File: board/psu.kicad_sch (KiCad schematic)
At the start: 38 parts, among them J1 BARREL_JACK, U1 LTC3374-QFN

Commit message: Continued initial schematic capture
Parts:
- J1: footprint (none) -> azonenberg_pcb:CONN_CUI_PJ-058BH_HIPWR_BARREL_NOSLOT
- R1, R2, R3, R4, R5, R6, R7, R8, R9: footprint (none) -> azonenberg_pcb:EIA_0402_RES_NOSILK
- TP1, TP2: footprint (none) -> azonenberg_pcb:TESTPOINT_SMT_0.5MM
- TP3, TP4, TP5, TP6, TP7: footprint (none) -> azonenberg_pcb:CONN_U.FL_TE_1909763-1
- TP8: footprint (none) -> azonenberg_pcb:TESTPOINT_SMT_KEYSTONE_5016
- U1: footprint (none) -> azonenberg_pcb:QFN_38_0.5MM_5x7MM
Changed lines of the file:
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@@
     (property "Reference" "TP8" (id 0) (at 215.9 123.1605 0))
     (property "Value" "TESTCLIP" (id 1) (at 215.9 125.9356 0))
-    (property "Footprint" "" (id 2) (at 215.9 128.27 0)
+    (property "Footprint" "azonenberg_pcb:TESTPOINT_SMT_KEYSTONE_5016" (id 2) (at 215.9 128.27 0)
       (effects (font (size 1.27 1.27)) hide)
     )
@@
       (effects (font (size 1.524 1.524)))
     )
-    (property "Footprint" "" (id 2) (at 43.18 34.29 0)
+    (property "Footprint" "azonenberg_pcb:QFN_38_0.5MM_5x7MM" (id 2) (at 43.18 34.29 0)
       (effects (font (size 1.524 1.524)) hide)
     )
@@
       (effects (font (size 1.524 1.524)))
     )
-    (property "Footprint" "" (id 2) (at 43.18 176.53 0)
+    (property "Footprint" "azonenberg_pcb:QFN_38_0.5MM_5x7MM" (id 2) (at 43.18 176.53 0)
       (effects (font (size 1.524 1.524)) hide)
     )
@@
       (effects (font (size 1.27 1.27)) (justify left))
     )
-    (property "Footprint" "" (id 2) (at 191.77 158.75 0)
+    (property "Footprint" "azonenberg_pcb:CONN_U.FL_TE_1909763-1" (id 2) (at 191.77 158.75 0)
       (effects (font (size 1.27 1.27)) hide)
     )
@@
     (property "Reference" "R5" (id 0) (at 71.12 114.3 0))
     (property "Value" "806K" (id 1) (at 71.12 116.84 0))
-    (property "Footprint" "" (id 2) (at 77.978 115.57 90)
+    (property "Footprint" "azonenberg_pcb:EIA_0402_RES_NOSILK" (id 2) (at 77.978 115.57 90)
       (effects (font (size 1.27 1.27)) hide)
     )
@@
     (property "Reference" "R1" (id 0) (at 71.12 33.02 0))
     (property "Value" "255K" (id 1) (at 71.12 35.56 0))
-    (property "Footprint" "" (id 2) (at 77.978 34.29 90)
+    (property "Footprint" "azonenberg_pcb:EIA_0402_RES_NOSILK" (id 2) (at 77.978 34.29 90)
       (effects (font (size 1.27 1.27)) hide)
     )
@@
     (property "Reference" "R8" (id 0) (at 71.12 162.56 0))
     (property "Value" "324K" (id 1) (at 71.12 165.1 0))
-    (property "Footprint" "" (id 2) (at 77.978 163.83 90)
+    (property "Footprint" "azonenberg_pcb:EIA_0402_RES_NOSILK" (id 2) (at 77.978 163.83 90)
       (effects (font (size 1.27 1.27)) hide)
     )
@@
     (property "Reference" "J1" (id 0) (at 175.895 17.7505 0))
     (property "Value" "BARREL_JACK" (id 1) (at 175.895 20.5256 0))
-    (property "Footprint" "" (id 2) (at 180.34 29.21 0)
+    (property "Footprint" "azonenberg_pcb:CONN_CUI_PJ-058BH_HIPWR_BARREL_NOSLOT" (id 2) (at 180.34 29.21 0)
       (effects (font (size 1.27 1.27)) hide)
     )
@@
     (property "Reference" "R9" (id 0) (at 201.93 114.3975 90))
     (property "Value" "10K" (id 1) (at 201.93 117.1726 90))
-    (property "Footprint" "" (id 2) (at 201.93 121.158 90)
+    (property "Footprint" "azonenberg_pcb:EIA_0402_RES_NOSILK" (id 2) (at 201.93 121.158 90)
       (effects (font (size 1.27 1.27)) hide)
     )
@@
       (effects (font (size 1.524 1.524)))
     )
-    (property "Footprint" "" (id 2) (at 43.18 156.21 0)
+    (property "Footprint" "azonenberg_pcb:QFN_38_0.5MM_5x7MM" (id 2) (at 43.18 156.21 0)
       (effects (font (size 1.524 1.524)) hide)
     )
@@
       (effects (font (size 1.524 1.524)))
     )
-    (property "Footprint" "" (id 2) (at 43.18 115.57 0)
+    (property "Footprint" "azonenberg_pcb:QFN_38_0.5MM_5x7MM" (id 2) (at 43.18 115.57 0)
       (effects (font (size 1.524 1.524)) hide)
     )
@@
       (effects (font (size 1.524 1.524)))
     )
-    (property "Footprint" "" (id 2) (at 43.18 54.61 0)
+    (property "Footprint" "azonenberg_pcb:QFN_38_0.5MM_5x7MM" (id 2) (at 43.18 54.61 0)
       (effects (font (size 1.524 1.524)) hide)
     )
@@
     (property "Reference" "R7" (id 0) (at 71.12 154.94 0))
     (property "Value" "1.02M" (id 1) (at 71.12 157.48 0))
-    (property "Footprint" "" (id 2) (at 77.978 156.21 90)
+    (property "Footprint" "azonenberg_pcb:EIA_0402_RES_NOSILK" (id 2) (at 77.978 156.21 90)
       (effects (font (size 1.27 1.27)) hide)
     )
@@
     (property "Reference" "TP2" (id 0) (at 184.15 123.1605 0))
     (property "Value" "TESTPOINT" (id 1) (at 184.15 125.9356 0))
-    (property "Footprint" "" (id 2) (at 184.15 128.27 0)
+    (property "Footprint" "azonenberg_pcb:TESTPOINT_SMT_0.5MM" (id 2) (at 184.15 128.27 0)
       (effects (font (size 1.27 1.27)) hide)
     )
@@
       (effects (font (size 1.27 1.27)) (justify left))
     )
-    (property "Footprint" "" (id 2) (at 191.77 168.91 0)
+    (property "Footprint" "azonenberg_pcb:CONN_U.FL_TE_1909763-1" (id 2) (at 191.77 168.91 0)
       (effects (font (size 1.27 1.27)) hide)
     )
@@
       (effects (font (size 1.27 1.27)) (justify left))
     )
-    (property "Footprint" "" (id 2) (at 191.77 179.07 0)
+    (property "Footprint" "azonenberg_pcb:CONN_U.FL_TE_1909763-1" (id 2) (at 191.77 179.07 0)
       (effects (font (size 1.27 1.27)) hide)
     )
@@
     (property "Reference" "TP1" (id 0) (at 184.15 114.2705 0))
     (property "Value" "TESTPOINT" (id 1) (at 184.15 117.0456 0))
-    (property "Footprint" "" (id 2) (at 184.15 119.38 0)
+    (property "Footprint" "azonenberg_pcb:TESTPOINT_SMT_0.5MM" (id 2) (at 184.15 119.38 0)
       (effects (font (size 1.27 1.27)) hide)
     )
@@
     (property "Reference" "R4" (id 0) (at 71.12 81.28 0))
     (property "Value" "464K" (id 1) (at 71.12 83.82 0))
-    (property "Footprint" "" (id 2) (at 77.978 82.55 90)
+    (property "Footprint" "azonenberg_pcb:EIA_0402_RES_NOSILK" (id 2) (at 77.978 82.55 90)
       (effects (font (size 1.27 1.27)) hide)
     )
@@
       (effects (font (size 1.524 1.524)))
     )
-    (property "Footprint" "" (id 2) (at 43.18 135.89 0)
+    (property "Footprint" "azonenberg_pcb:QFN_38_0.5MM_5x7MM" (id 2) (at 43.18 135.89 0)
       (effects (font (size 1.524 1.524)) hide)
     )
@@
       (effects (font (size 1.524 1.524)))
     )
-    (property "Footprint" "" (id 2) (at 43.18 74.93 0)
+    (property "Footprint" "azonenberg_pcb:QFN_38_0.5MM_5x7MM" (id 2) (at 43.18 74.93 0)
       (effects (font (size 1.524 1.524)) hide)
     )
@@
       (effects (font (size 1.27 1.27)) (justify left))
     )
-    (property "Footprint" "" (id 2) (at 191.77 148.59 0)
+    (property "Footprint" "azonenberg_pcb:CONN_U.FL_TE_1909763-1" (id 2) (at 191.77 148.59 0)
       (effects (font (size 1.27 1.27)) hide)
     )
@@
       (effects (font (size 1.524 1.524)))
     )
-    (property "Footprint" "" (id 2) (at 43.18 95.25 0)
+    (property "Footprint" "azonenberg_pcb:QFN_38_0.5MM_5x7MM" (id 2) (at 43.18 95.25 0)
       (effects (font (size 1.524 1.524)) hide)
     )
@@
       (effects (font (size 1.27 1.27)) (justify left))
     )
-    (property "Footprint" "" (id 2) (at 191.77 138.43 0)
+    (property "Footprint" "azonenberg_pcb:CONN_U.FL_TE_1909763-1" (id 2) (at 191.77 138.43 0)
       (effects (font (size 1.27 1.27)) hide)
     )
@@
     (property "Reference" "R3" (id 0) (at 71.12 73.66 0))
     (property "Value" "232K" (id 1) (at 71.12 76.2 0))
-    (property "Footprint" "" (id 2) (at 77.978 74.93 90)
+    (property "Footprint" "azonenberg_pcb:EIA_0402_RES_NOSILK" (id 2) (at 77.978 74.93 90)
       (effects (font (size 1.27 1.27)) hide)
     )
@@
     (property "Reference" "R6" (id 0) (at 71.12 121.92 0))
     (property "Value" "649K" (id 1) (at 71.12 124.46 0))
-    (property "Footprint" "" (id 2) (at 77.978 123.19 90)
+    (property "Footprint" "azonenberg_pcb:EIA_0402_RES_NOSILK" (id 2) (at 77.978 123.19 90)
       (effects (font (size 1.27 1.27)) hide)
     )
@@
       (effects (font (size 1.524 1.524)))
     )
-    (property "Footprint" "" (id 2) (at 138.43 34.29 0)
+    (property "Footprint" "azonenberg_pcb:QFN_38_0.5MM_5x7MM" (id 2) (at 138.43 34.29 0)
       (effects (font (size 1.524 1.524)) hide)
     )
@@
     (property "Reference" "R2" (id 0) (at 71.12 40.64 0))
     (property "Value" "1.02M" (id 1) (at 71.12 43.18 0))
-    (property "Footprint" "" (id 2) (at 77.978 41.91 90)
-      (effects (font (size 1.27 1.27)) hide)
-    )
+    (property "Footprint" "azonenberg_pcb:EIA_0402_RES_NOSILK" (id 2) (at 77.978 41.91 90)
+      (effects (font (size 1.27 1.27)) hide)
+    )

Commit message: Finished initial schematic, ready for signoff review
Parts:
- C1, C10, C11, C12, C13, C14, C2, C4, C6, C7, C8, C9: footprint (none) -> azonenberg_pcb:EIA_1210_CAP_NOSILK
- C3, C5: footprint (none) -> azonenberg_pcb:EIA_1206_CAP_NOSILK
- F1: footprint (none) -> azonenberg_pcb:EIA_0603_CAP_NOSILK
- L1, L2, L3, L4: footprint (none) -> azonenberg_pcb:INDUCTOR_YUDEN_NRS5030
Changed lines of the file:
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@@
       (effects (font (size 1.27 1.27)) (justify left))
     )
-    (property "Footprint" "" (id 2) (at 82.2452 160.02 0)
+    (property "Footprint" "azonenberg_pcb:EIA_1210_CAP_NOSILK" (id 2) (at 82.2452 160.02 0)
       (effects (font (size 1.27 1.27)) hide)
     )
@@
       (effects (font (size 1.016 1.016)))
     )
-    (property "Footprint" "" (id 2) (at 64.77 71.12 0)
+    (property "Footprint" "azonenberg_pcb:INDUCTOR_YUDEN_NRS5030" (id 2) (at 64.77 71.12 0)
       (effects (font (size 1.524 1.524)) hide)
     )
@@
       (effects (font (size 1.27 1.27)) (justify left))
     )
-    (property "Footprint" "" (id 2) (at 89.8652 190.5 0)
+    (property "Footprint" "azonenberg_pcb:EIA_1210_CAP_NOSILK" (id 2) (at 89.8652 190.5 0)
       (effects (font (size 1.27 1.27)) hide)
     )
@@
       (effects (font (size 1.27 1.27)) (justify left))
     )
-    (property "Footprint" "" (id 2) (at 82.2452 78.74 0)
+    (property "Footprint" "azonenberg_pcb:EIA_1210_CAP_NOSILK" (id 2) (at 82.2452 78.74 0)
       (effects (font (size 1.27 1.27)) hide)
     )
@@
       (effects (font (size 1.27 1.27)) (justify left))
     )
-    (property "Footprint" "" (id 2) (at 55.5752 190.5 0)
+    (property "Footprint" "azonenberg_pcb:EIA_1210_CAP_NOSILK" (id 2) (at 55.5752 190.5 0)
       (effects (font (size 1.27 1.27)) hide)
     )
@@
       (effects (font (size 1.27 1.27)) (justify left))
     )
-    (property "Footprint" "" (id 2) (at 207.9752 30.48 0)
+    (property "Footprint" "azonenberg_pcb:EIA_1206_CAP_NOSILK" (id 2) (at 207.9752 30.48 0)
       (effects (font (size 1.27 1.27)) hide)
     )
@@
       (effects (font (size 1.27 1.27)) (justify left))
     )
-    (property "Footprint" "" (id 2) (at 32.7152 190.5 0)
+    (property "Footprint" "azonenberg_pcb:EIA_1210_CAP_NOSILK" (id 2) (at 32.7152 190.5 0)
       (effects (font (size 1.27 1.27)) hide)
     )
@@
       (effects (font (size 1.27 1.27)) (justify left))
     )
-    (property "Footprint" "" (id 2) (at 21.2852 190.5 0)
+    (property "Footprint" "azonenberg_pcb:EIA_1210_CAP_NOSILK" (id 2) (at 21.2852 190.5 0)
       (effects (font (size 1.27 1.27)) hide)
     )
@@
       (effects (font (size 1.27 1.27)) (justify left))
     )
-    (property "Footprint" "" (id 2) (at 112.7252 190.5 0)
+    (property "Footprint" "azonenberg_pcb:EIA_1210_CAP_NOSILK" (id 2) (at 112.7252 190.5 0)
       (effects (font (size 1.27 1.27)) hide)
     )
@@
       (effects (font (size 1.27 1.27)) (justify left))
     )
-    (property "Footprint" "" (id 2) (at 82.2452 38.1 0)
+    (property "Footprint" "azonenberg_pcb:EIA_1210_CAP_NOSILK" (id 2) (at 82.2452 38.1 0)
       (effects (font (size 1.27 1.27)) hide)
     )
@@
       (effects (font (size 1.27 1.27)) (justify left))
     )
-    (property "Footprint" "" (id 2) (at 67.0052 190.5 0)
+    (property "Footprint" "azonenberg_pcb:EIA_1210_CAP_NOSILK" (id 2) (at 67.0052 190.5 0)
       (effects (font (size 1.27 1.27)) hide)
     )
@@
       (effects (font (size 1.27 1.27)) (justify left))
     )
-    (property "Footprint" "" (id 2) (at 82.2452 119.38 0)
+    (property "Footprint" "azonenberg_pcb:EIA_1206_CAP_NOSILK" (id 2) (at 82.2452 119.38 0)
       (effects (font (size 1.27 1.27)) hide)
     )
@@
       (effects (font (size 1.016 1.016)))
     )
-    (property "Footprint" "" (id 2) (at 64.77 152.4 0)
+    (property "Footprint" "azonenberg_pcb:INDUCTOR_YUDEN_NRS5030" (id 2) (at 64.77 152.4 0)
       (effects (font (size 1.524 1.524)) hide)
     )
@@
       (effects (font (size 1.27 1.27)) (justify left))
     )
-    (property "Footprint" "" (id 2) (at 101.2952 190.5 0)
+    (property "Footprint" "azonenberg_pcb:EIA_1210_CAP_NOSILK" (id 2) (at 101.2952 190.5 0)
       (effects (font (size 1.27 1.27)) hide)
     )
@@
       (effects (font (size 1.27 1.27)) (justify left))
     )
-    (property "Footprint" "" (id 2) (at 44.1452 190.5 0)
+    (property "Footprint" "azonenberg_pcb:EIA_1210_CAP_NOSILK" (id 2) (at 44.1452 190.5 0)
       (effects (font (size 1.27 1.27)) hide)
     )
@@
       (effects (font (size 1.016 1.016)))
     )
-    (property "Footprint" "" (id 2) (at 64.77 30.48 0)
+    (property "Footprint" "azonenberg_pcb:INDUCTOR_YUDEN_NRS5030" (id 2) (at 64.77 30.48 0)
       (effects (font (size 1.524 1.524)) hide)
     )
@@
       (effects (font (size 1.27 1.27)) (justify left))
     )
-    (property "Footprint" "" (id 2) (at 78.4352 190.5 0)
+    (property "Footprint" "azonenberg_pcb:EIA_1210_CAP_NOSILK" (id 2) (at 78.4352 190.5 0)
       (effects (font (size 1.27 1.27)) hide)
     )
@@
       (effects (font (size 1.016 1.016)))
     )
-    (property "Footprint" "" (id 2) (at 64.77 111.76 0)
+    (property "Footprint" "azonenberg_pcb:INDUCTOR_YUDEN_NRS5030" (id 2) (at 64.77 111.76 0)
       (effects (font (size 1.524 1.524)) hide)
     )
@@
     (property "Reference" "F1" (id 0) (at 203.2 18.3855 0))
     (property "Value" "2A" (id 1) (at 203.2 21.1606 0))
-    (property "Footprint" "" (id 2) (at 205.105 22.86 0)
-      (effects (font (size 1.524 1.524)) hide)
-    )
+    (property "Footprint" "azonenberg_pcb:EIA_0603_CAP_NOSILK" (id 2) (at 205.105 22.86 0)
+      (effects (font (size 1.524 1.524)) hide)
+    )

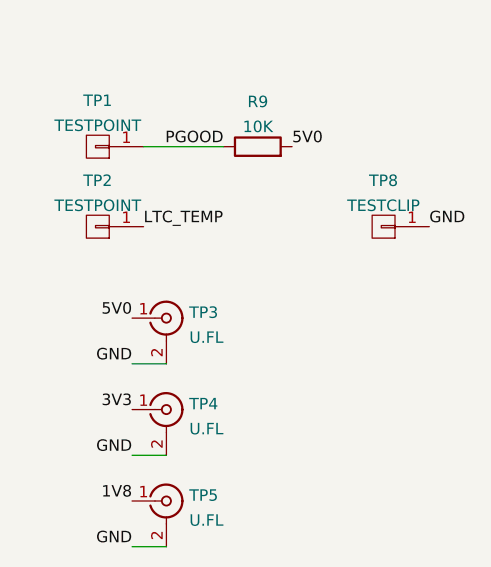
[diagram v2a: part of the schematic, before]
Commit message: Finished schematic review. Added a few more test points.
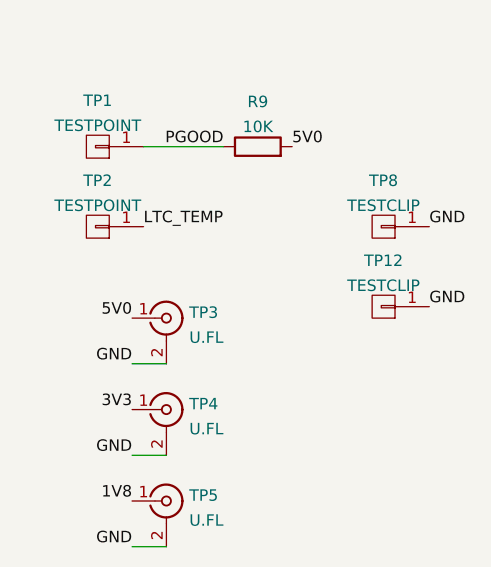
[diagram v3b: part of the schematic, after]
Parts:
- added TP12: TESTCLIP, azonenberg_pcb:TESTPOINT_SMT_KEYSTONE_5016, symbol conn:CONN_01X01
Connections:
- net GND: now also TP12.1 (P1)
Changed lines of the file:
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@@
+    (effects (font (size 1.27 1.27)) (justify left bottom))
+  )
+  (label "GND" (at 220.98 137.16 0)
     (effects (font (size 1.27 1.27)) (justify left bottom))
   )
@@
     (pin "2")
   )
+  (symbol (lib_id "conn:CONN_01X01") (at 215.9 137.16 180) (unit 1)
+    (in_bom yes) (on_board yes) (fields_autoplaced)
+    (property "Reference" "TP12" (id 0) (at 215.9 132.0505 0))
+    (property "Value" "TESTCLIP" (id 1) (at 215.9 134.8256 0))
+    (property "Footprint" "azonenberg_pcb:TESTPOINT_SMT_KEYSTONE_5016" (id 2) (at 215.9 137.16 0)
+      (effects (font (size 1.27 1.27)) hide)
+    )
+    (property "Datasheet" "" (id 3) (at 215.9 137.16 0)
+      (effects (font (size 1.27 1.27)) hide)
+    )
+    (pin "1")
+  )
   (symbol (lib_id "passive-azonenberg:INDUCTOR_PWROUT") (at 64.77 30.48 270) (unit 1)

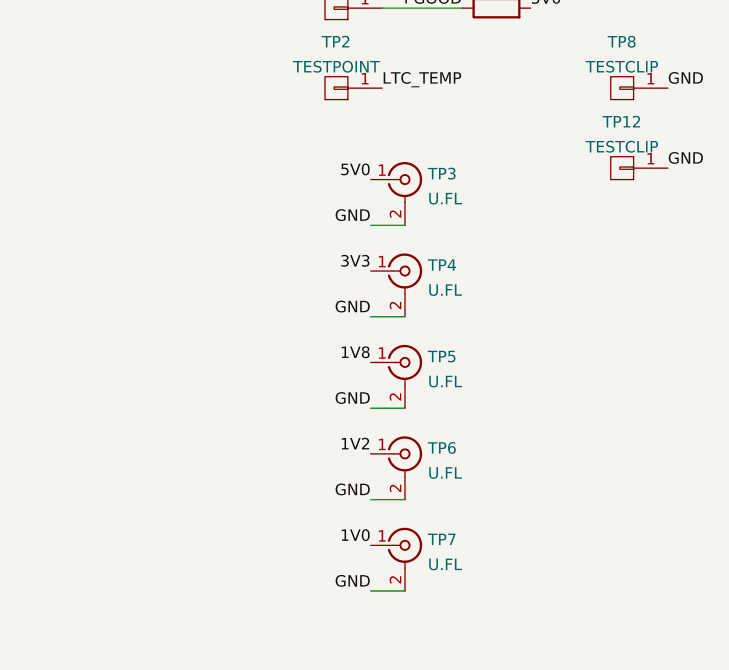
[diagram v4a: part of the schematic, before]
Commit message: Finished power supply layout, added mounting holes and a bunch of silkscreen labeling
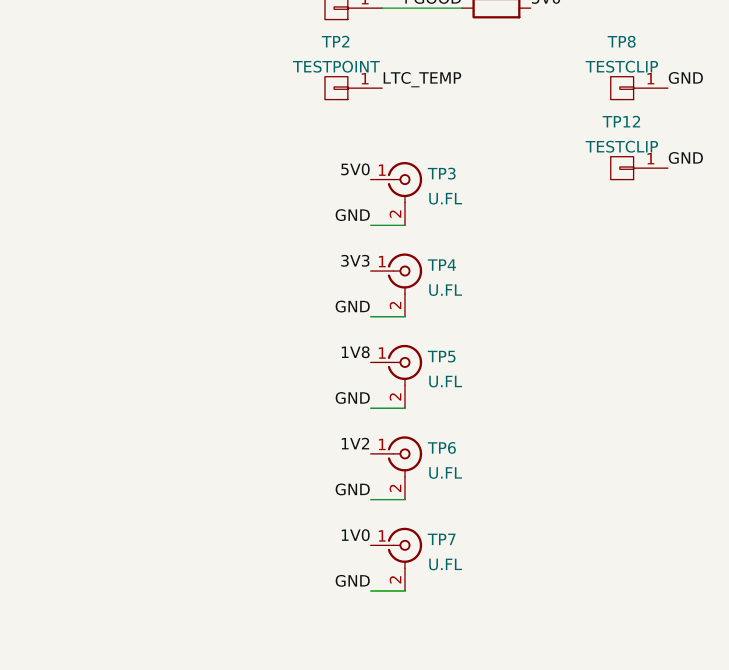
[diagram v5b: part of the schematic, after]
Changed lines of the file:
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@@
   (title_block
     (title "Active 10/100/1000baseT Tap")
-    (date "2022-12-21")
+    (date "2022-12-23")
     (rev "0.1")
     (company "Antikernel Labs")
